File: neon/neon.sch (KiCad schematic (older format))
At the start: 30 parts, among them J1 V3V3-VIO, J2 3xV3V3-GND, J5 VBUS-VCC, U2 C, U3 B, U4 A, U5 D, U6 74HC595

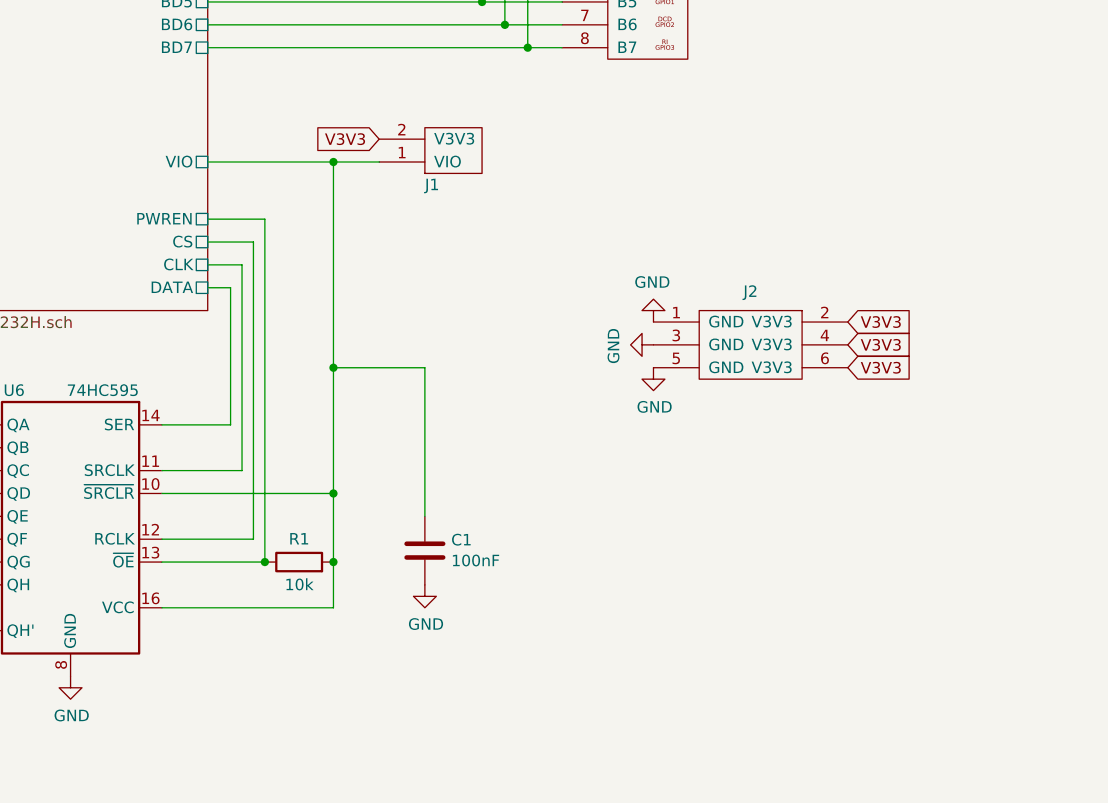
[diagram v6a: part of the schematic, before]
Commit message: Fix nets width
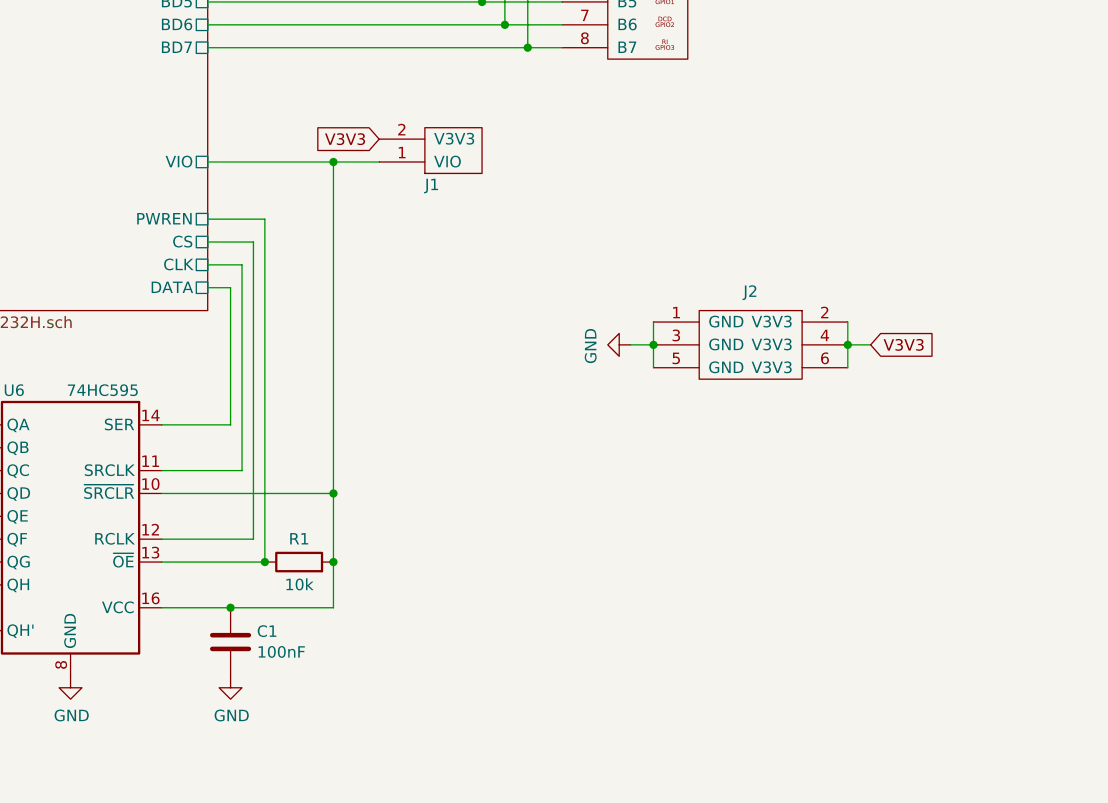
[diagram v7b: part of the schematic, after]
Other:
- moved on the sheet: C1
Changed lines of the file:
@@
 	6400 4300 6950 4300
-Wire Wire Line
-	6950 4300 6950 5200
 Wire Wire Line
 	4400 4200 5200 4200
@@
 NoConn ~ 5400 6350
 Wire Wire Line
-	6200 6250 6950 6250
+	6200 6250 6500 6250
 Connection ~ 7800 3800
 Wire Wire Line
@@
 L power:GND #PWR02
 U 1 1 5F6FFFFA
-P 7350 6150
-F 0 "#PWR02" H 7350 5900 50  0001 C CNN
-F 1 "GND" H 7355 5977 50  0000 C CNN
-F 2 "" H 7350 6150 50  0001 C CNN
-F 3 "" H 7350 6150 50  0001 C CNN
-	1    7350 6150
+P 6500 6550
+F 0 "#PWR02" H 6500 6300 50  0001 C CNN
+F 1 "GND" H 6505 6377 50  0000 C CNN
+F 2 "" H 6500 6550 50  0001 C CNN
+F 3 "" H 6500 6550 50  0001 C CNN
+	1    6500 6550
 	1    0    0    -1
 $EndComp
@@
 L Device:C C1
 U 1 1 5F6FF541
-P 7350 6000
-F 0 "C1" H 7465 6046 50  0000 L CNN
-F 1 "100nF" H 7465 5955 50  0000 L CNN
-F 2 "Capacitor_SMD:C_0805_2012Metric" H 7388 5850 50  0001 C CNN
-F 3 "~" H 7350 6000 50  0001 C CNN
-	1    7350 6000
-	1    0    0    -1
-$EndComp
-Wire Wire Line
-	6950 5200 7350 5200
-Wire Wire Line
-	7350 5200 7350 5850
-Connection ~ 6950 5200
-Wire Wire Line
-	6950 5200 6950 5750
-$Comp
-L FTDI:3xV3V3-GND J2
-U 1 1 5F5754BA
-P 8650 5000
-F 0 "J2" H 8775 5133 50  0000 C CNN
-F 1 "3xV3V3-GND" H 8800 4700 50  0001 C CNN
-F 2 "Connector_PinHeader_2.54mm:PinHeader_2x03_P2.54mm_Vertical" H 8650 5000 50  0001 C CNN
-F 3 "~" H 8650 5000 50  0001 C CNN
-	1    8650 5000
+P 6500 6400
+F 0 "C1" H 6615 6446 50  0000 L CNN
+F 1 "100nF" H 6615 6355 50  0000 L CNN
+F 2 "Capacitor_SMD:C_0805_2012Metric" H 6538 6250 50  0001 C CNN
+F 3 "~" H 6500 6400 50  0001 C CNN
+	1    6500 6400
 	1    0    0    -1
 $EndComp
@@
 L power:GND #PWR05
 U 1 1 5F576283
-P 8350 5200
-F 0 "#PWR05" H 8350 4950 50  0001 C CNN
-F 1 "GND" H 8355 5027 50  0000 C CNN
-F 2 "" H 8350 5200 50  0001 C CNN
-F 3 "" H 8350 5200 50  0001 C CNN
-	1    8350 5200
-	1    0    0    -1
-$EndComp
-$Comp
-L power:GND #PWR03
-U 1 1 5F5907B8
-P 8350 5000
-F 0 "#PWR03" H 8350 4750 50  0001 C CNN
-F 1 "GND" H 8355 4827 50  0000 C CNN
-F 2 "" H 8350 5000 50  0001 C CNN
-F 3 "" H 8350 5000 50  0001 C CNN
-	1    8350 5000
-	-1   0    0    1
-$EndComp
-$Comp
-L power:GND #PWR04
-U 1 1 5F590D03
-P 8350 5100
-F 0 "#PWR04" H 8350 4850 50  0001 C CNN
-F 1 "GND" H 8355 4927 50  0000 C CNN
-F 2 "" H 8350 5100 50  0001 C CNN
-F 3 "" H 8350 5100 50  0001 C CNN
-	1    8350 5100
+P 8250 5100
+F 0 "#PWR05" H 8250 4850 50  0001 C CNN
+F 1 "GND" H 8255 4927 50  0000 C CNN
+F 2 "" H 8250 5100 50  0001 C CNN
+F 3 "" H 8250 5100 50  0001 C CNN
+	1    8250 5100
 	0    1    1    0
 $EndComp
-Text GLabel 9200 5000 2    50   Input ~ 0
-V3V3
-Text GLabel 9200 5100 2    50   Input ~ 0
-V3V3
-Text GLabel 9200 5200 2    50   Input ~ 0
-V3V3
 $Comp
 L Device:LED D1
@@
 Wire Wire Line
 	3200 5350 3200 5000
+Wire Wire Line
+	8350 5000 8350 5100
+Connection ~ 8350 5100
+Wire Wire Line
+	8350 5100 8350 5200
+Wire Wire Line
+	9200 5000 9200 5100
+Connection ~ 9200 5100
+Wire Wire Line
+	9200 5100 9200 5200
+Text GLabel 9300 5100 2    50   Input ~ 0
+V3V3
+$Comp
+L FTDI:3xV3V3-GND J2
+U 1 1 5F5754BA
+P 8650 5000
+F 0 "J2" H 8775 5133 50  0000 C CNN
+F 1 "3xV3V3-GND" H 8800 4700 50  0001 C CNN
+F 2 "Connector_PinHeader_2.54mm:PinHeader_2x03_P2.54mm_Vertical" H 8650 5000 50  0001 C CNN
+F 3 "~" H 8650 5000 50  0001 C CNN
+	1    8650 5000
+	1    0    0    -1
+$EndComp
+Wire Wire Line
+	9300 5100 9200 5100
+Wire Wire Line
+	8350 5100 8250 5100
+Connection ~ 6500 6250
+Wire Wire Line
+	6500 6250 6950 6250
+Wire Wire Line
+	6950 4300 6950 5750
 $EndSCHEMATC
